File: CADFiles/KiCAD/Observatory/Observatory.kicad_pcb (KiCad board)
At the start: 2 copper layers, 204.4 x 77 mm, 49 parts, among them J1 GND/CUT, J10 Dio_Jump, J11 nRF Connections, J12 Sulu Header, J13 Dio_AD, J14 RsTx_Dio, J15 RsRx_Dio, J16 JScope Voltage, J17 WaveGen. 1 Mux Config., J18 JScope I+, J19 JScope I-, J2 Analog Discovery Connection, J20 Mounting Hole, J21 Mounting Hole, J22 Mounting Hole, J23 Mounting Hole, J24 prog. LED, J3 Digitial Discovery Connection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, J4 Scope 1 Mux Config., J5 Scope 2 Mux Config., J6 JScope V+, J7 JScope V-, J8 JScope Current IO, J9 5V_in, Q1 2N7002, U1 1, U2 Scope 1 Mux, U3 Wave Gen. Mux, U4 Scope 2 Mux

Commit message: Begin REV 2
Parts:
- removed 10k: 100k, Resistor_SMD:R_0805_2012Metric_Pad1.20x1.40mm_HandSolder
- removed J13: Dio_AD, Connector_PinHeader_2.54mm:PinHeader_2x16_P2.54mm_Vertical
- added R17: 100k, Resistor_SMD:R_0805_2012Metric_Pad1.20x1.40mm_HandSolder, F.Cu at (140.5, 31.5)
- added SW1: SW_DIP_x08, Button_Switch_THT:SW_DIP_SPSTx08_Slide_9.78x22.5mm_W7.62mm_P2.54mm, F.Cu at (210.5, 53.7)
- added SW2: SW_DIP_x08, Button_Switch_THT:SW_DIP_SPSTx08_Slide_9.78x22.5mm_W7.62mm_P2.54mm, F.Cu at (210.5, 83.5)
- added U5: Pico, 3rdPrty_Footprints:RPi_Pico_SMD_TH, B.Cu at (73.6, 90.5)
- J1: moved to F.Cu
- J16: value JScope Voltage -> JScope Voltage Select
- moved R13 160.0 mm to (217.8, 26.0), turned to -90 degrees
- moved R12 158.1 mm to (214.9, 26.0), turned to -90 degrees
- moved R11 156.5 mm to (211.9, 26.0), turned to -90 degrees
- moved R10 155.0 mm to (209.0, 26.0), turned to -90 degrees
- moved R9 153.7 mm to (206.1, 26.0), turned to -90 degrees
- moved R8 152.6 mm to (203.1, 26.0), turned to -90 degrees
- moved R7 151.8 mm to (200.2, 26.0), turned to -90 degrees
- moved R6 151.1 mm to (197.2, 26.0), turned to -90 degrees
- moved R5 150.6 mm to (194.3, 26.0), turned to -90 degrees
- moved R2 150.3 mm to (185.4, 26.0), turned to -90 degrees
- moved R4 150.3 mm to (191.3, 26.0), turned to -90 degrees
- moved R3 150.2 mm to (188.4, 26.0), turned to -90 degrees
- moved R16 122.6 mm to (182.4, 26.0), turned to -90 degrees
- moved R15 120.5 mm to (179.5, 26.0), turned to -90 degrees
- moved R14 118.6 mm to (176.6, 26.0), turned to -90 degrees
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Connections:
- J1 pad 1: JS_V- -> AD_Scope1-
- J10 pad 1: Scope 1 Mux  1 -> Scope 1 Mux  2
- J10 pad 2: DD_DIN_1 -> DD_DIN_0
- J10 pad 3: Scope 1 Mux  2 -> Scope 1 Mux  1
- J10 pad 4: DD_DIN_0 -> DD_DIN_1
- J11 pad 1: JS_V- -> AD_Scope1-
- J12 pad 1: JS_V- -> AD_Scope1-
- J12 pad 11: JS_V- -> AD_Scope1-
- J12 pad 2: JS_V- -> AD_Scope1-
- J12 pad 3: JS_V- -> AD_Scope1-
- J14 pad 2: DD_DIN_1 -> DD_DIN_0
- J15 pad 2: DD_DIN_0 -> DD_DIN_1
- J17 pad 1: JS_V- -> AD_Scope1-
- J17 pad 2: JS_V- -> AD_Scope1-
- J17 pad 3: JS_V- -> AD_Scope1-
- J17 pad 4: JS_V- -> AD_Scope1-
- J17 pad 5: JS_V- -> AD_Scope1-
- J2 pad 11: JS_V- -> AD_Scope1-
- J2 pad 12: JS_V- -> AD_Scope1-
- J2 pad 4: AD_Scope2- -> AD_Scope1-
- J2 pad 5: JS_V- -> AD_Scope1-
- J2 pad 6: JS_V- -> AD_Scope1-
- J3 pad 1: JS_V- -> AD_Scope1-
- J3 pad 11: JS_V- -> AD_Scope1-
- J3 pad 12: JS_V- -> AD_Scope1-
- J3 pad 2: JS_V- -> AD_Scope1-
- J3 pad 21: JS_V- -> AD_Scope1-
- J3 pad 22: JS_V- -> AD_Scope1-
- J3 pad 31: JS_V- -> AD_Scope1-
- J3 pad 32: JS_V- -> AD_Scope1-
- J4 pad 1: JS_V- -> AD_Scope1-
- J4 pad 2: JS_V- -> AD_Scope1-
- J4 pad 3: JS_V- -> AD_Scope1-
- J4 pad 4: JS_V- -> AD_Scope1-
- J4 pad 5: JS_V- -> AD_Scope1-
- J5 pad 1: JS_V- -> AD_Scope1-
- J5 pad 2: JS_V- -> AD_Scope1-
- J5 pad 3: JS_V- -> AD_Scope1-
- J5 pad 4: JS_V- -> AD_Scope1-
- J5 pad 5: JS_V- -> AD_Scope1-
- J7 pad 2: JS_V- -> AD_Scope1-
- J9 pad 1: JS_V- -> AD_Scope1-
- U1 pad 10b: JS_V- -> AD_Scope1-
- U1 pad 11c: JS_V- -> AD_Scope1-
- U1 pad 19a: JS_V- -> AD_Scope1-
- U1 pad 1a: JS_V- -> AD_Scope1-
- U1 pad 1c: JS_V- -> AD_Scope1-
- U1 pad 20a: JS_V- -> AD_Scope1-
- U1 pad 2c: JS_V- -> AD_Scope1-
- U1 pad 3b: JS_V- -> AD_Scope1-
- U1 pad 3c: JS_V- -> AD_Scope1-
- U2 pad 20: JS_V- -> AD_Scope1-
- U2 pad 21: JS_V- -> AD_Scope1-
- U2 pad 22: JS_V- -> AD_Scope1-
- U2 pad 23: JS_V- -> AD_Scope1-
- U2 pad 24: JS_V- -> AD_Scope1-
- U3 pad 1: Scope 1 Mux  1 -> Scopes Mux  1
- U3 pad 10: Scope 1 Mux  10 -> Scopes Mux  10
- U3 pad 11: Scope 1 Mux  11 -> Scopes Mux  11
- U3 pad 12: Scope 1 Mux  12 -> Scopes Mux  12
- U3 pad 2: Scope 1 Mux  2 -> Scopes Mux  2
- U3 pad 20: JS_V- -> AD_Scope1-
- U3 pad 21: JS_V- -> AD_Scope1-
- U3 pad 22: JS_V- -> AD_Scope1-
- U3 pad 23: JS_V- -> AD_Scope1-
- U3 pad 24: JS_V- -> AD_Scope1-
- U3 pad 3: Scope 1 Mux  3 -> Scopes Mux  3
- U3 pad 4: Scope 1 Mux  4 -> Scopes Mux  4
- U3 pad 45: Scope 1 Mux  16 -> Scopes Mux  16
- U3 pad 46: Scope 1 Mux  15 -> Scopes Mux  15
- U3 pad 47: Scope 1 Mux  14 -> Scopes Mux  14
- U3 pad 48: Scope 1 Mux  13 -> Scopes Mux  13
- U3 pad 5: Scope 1 Mux  5 -> Scopes Mux  5
- U3 pad 6: Scope 1 Mux  6 -> Scopes Mux  6
- U3 pad 7: Scope 1 Mux  7 -> Scopes Mux  7
- U3 pad 8: Scope 1 Mux  8 -> Scopes Mux  8
- U3 pad 9: Scope 1 Mux  9 -> Scopes Mux  9
- U4 pad 20: JS_V- -> AD_Scope1-
- U4 pad 21: JS_V- -> AD_Scope1-
- U4 pad 22: JS_V- -> AD_Scope1-
- U4 pad 23: JS_V- -> AD_Scope1-
- U4 pad 24: JS_V- -> AD_Scope1-
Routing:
- net +5V: track 276.4 -> 0.00 mm, vias 15 -> 0
- net AD_Scope1+: track 228.5 -> 0.00 mm, vias 2 -> 0
- net Scope 1 Mux  12: track 225.2 -> 0.00 mm, vias 2 -> 0
- net AD_Scope2+: track 220.7 -> 0.00 mm, vias 2 -> 0
- net Scope 1 Mux  11: track 218.4 -> 0.00 mm, vias 2 -> 0
- net Scope 1 Mux  10: track 216.7 -> 0.00 mm, vias 2 -> 0
- net Scope 1 Mux  9: track 209.4 -> 0.00 mm, vias 2 -> 0
- net Scope 1 Mux  8: track 208.7 -> 0.00 mm, vias 2 -> 0
- net Scope 1 Mux  7: track 202.1 -> 0.00 mm, vias 2 -> 0
- net Scope 1 Mux  6: track 201.1 -> 0.00 mm, vias 2 -> 0
- net Scope 1 Mux  5: track 194.6 -> 0.00 mm, vias 2 -> 0
- net Scope 1 Mux  4: track 194.2 -> 0.00 mm, vias 2 -> 0
- net Scope 1 Mux  2: track 191.5 -> 0.00 mm, vias 2 -> 0
- net Scope 1 Mux  3: track 189.9 -> 0.00 mm, vias 2 -> 0
- net Scope 1 Mux  16: track 188.7 -> 0.00 mm, vias 4 -> 0
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- removed copper zone on B.Cu, net JS_V-
- removed copper zone on F.Cu, net JS_V-
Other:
- copper layers 2 -> 4
- board text removed: "+"
- board text removed: "-"
- board text removed: "->"
- board text removed: "1.1V"
- board text removed: "1.1V_IN"
- board text removed: "1.8V"
- board text removed: "3WB CLK"
- board text removed: "3WB DATA"
- board text removed: "3WB ENB"
- board text removed: "ADC IN"
- board text removed: "ADC OUT"
- board text removed: "BTSRC SEL"
- board text removed: "GND"
- board text removed: "HARD RESET"
- board text removed: "IMU VDD"
- board text removed: "IMU VDDIO"
- board text removed: "JScope Voltage"
- board text removed: "NRF GND"
- board text removed: "NRF VDDD"
- board text removed: "Single-Chip micro Mote Observatory"
- board text removed: "VBAT"
- board text removed: "VDDD"
- board text removed: "VDDIO"

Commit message: All nets routed.
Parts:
- added J13: Serial, Connector_PinHeader_2.54mm:PinHeader_1x02_P2.54mm_Vertical, F.Cu at (93.5, 107.9)
- C1, C2, J1, Q1, R1, R17: moved to B.Cu
- J16: value JScope Voltage Select -> JScope Voltage
- J17, J4, J5: footprint Imports:DIP8_208-5_CTS -> Button_Switch_SMD:SW_DIP_SPSTx05_Slide_6.7x14.26mm_W8.61mm_P2.54mm_LowProfile
- SW1, SW2: footprint Button_Switch_THT:SW_DIP_SPSTx08_Slide_9.78x22.5mm_W7.62mm_P2.54mm -> Button_Switch_SMD:SW_DIP_SPSTx08_Slide_6.7x21.88mm_W8.61mm_P2.54mm_LowProfile
- moved G*** 150.9 mm to (125.8, 78.1)
- moved U5 142.7 mm to (213.4, 61.9), turned to 180 degrees
- moved J4 117.6 mm to (151.1, 42.3), turned to -90 degrees
- moved R13 98.9 mm to (122.0, 50.2), turned to 90 degrees
- moved J5 93.8 mm to (134.6, 42.3), turned to -90 degrees
- moved R12 92.6 mm to (125.5, 50.2), turned to 90 degrees
- moved R11 86.7 mm to (128.7, 50.2), turned to 90 degrees
- moved R10 81.0 mm to (131.7, 50.2), turned to 90 degrees
- moved J1 78.4 mm to (75.3, 46.6), turned to 180 degrees
- moved J23 77.1 mm to (250.2, 40.2)
- moved R9 75.4 mm to (134.6, 50.2), turned to 90 degrees
- moved Q1 74.4 mm to (76.0, 50.2)
- moved R16 74.1 mm to (112.4, 50.1), turned to 90 degrees
- moved C1 73.2 mm to (71.4, 46.6), turned to 180 degrees
- moved C2 73.0 mm to (71.4, 49.0), turned to 180 degrees
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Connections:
- J1 pad 1: AD_Scope1- -> AD_DC_Supply-
- J10 pad 1: Scope 1 Mux  2 -> Scope 1 Mux  1
- J10 pad 13: Scope 1 Mux  7 -> Scope 1 Mux  12
- J10 pad 15: Scope 1 Mux  8 -> Scope 1 Mux  11
- J10 pad 17: Scope 1 Mux  9 -> Scope 1 Mux  10
- J10 pad 19: Scope 1 Mux  10 -> Scope 1 Mux  9
- J10 pad 21: Scope 1 Mux  11 -> Scope 1 Mux  8
- J10 pad 23: Scope 1 Mux  12 -> Scope 1 Mux  7
- J10 pad 3: Scope 1 Mux  1 -> Scope 1 Mux  2
- J11 pad 1: AD_Scope1- -> AD_DC_Supply-
- J12 pad 1: AD_Scope1- -> AD_DC_Supply-
- J12 pad 11: AD_Scope1- -> AD_DC_Supply-
- J12 pad 12: +5V -> AD_DC_Supply+
- J12 pad 2: AD_Scope1- -> AD_DC_Supply-
- J12 pad 3: AD_Scope1- -> AD_DC_Supply-
- J16 pad 5: +5V -> AD_DC_Supply+
- J17 pad 1: AD_Scope1- -> AD_DC_Supply-
- J17 pad 2: AD_Scope1- -> AD_DC_Supply-
- J17 pad 3: AD_Scope1- -> AD_DC_Supply-
- J17 pad 4: AD_Scope1- -> AD_DC_Supply-
- J17 pad 5: AD_Scope1- -> AD_DC_Supply-
- J2 pad 11: AD_Scope1- -> AD_DC_Supply-
- J2 pad 12: AD_Scope1- -> AD_DC_Supply-
- J2 pad 2: AD_Scope1- -> AD_DC_Supply-
- J2 pad 4: AD_Scope1- -> AD_DC_Supply-
- J2 pad 5: AD_Scope1- -> AD_DC_Supply-
- J2 pad 6: AD_Scope1- -> AD_DC_Supply-
- J3 pad 1: AD_Scope1- -> AD_DC_Supply-
- J3 pad 11: AD_Scope1- -> AD_DC_Supply-
- J3 pad 12: AD_Scope1- -> AD_DC_Supply-
- J3 pad 2: AD_Scope1- -> AD_DC_Supply-
- J3 pad 21: AD_Scope1- -> AD_DC_Supply-
- J3 pad 22: AD_Scope1- -> AD_DC_Supply-
- J3 pad 31: AD_Scope1- -> AD_DC_Supply-
- J3 pad 32: AD_Scope1- -> AD_DC_Supply-
- J4 pad 1: AD_Scope1- -> AD_DC_Supply-
- J4 pad 2: AD_Scope1- -> AD_DC_Supply-
- J4 pad 3: AD_Scope1- -> AD_DC_Supply-
- J4 pad 4: AD_Scope1- -> AD_DC_Supply-
- J4 pad 5: AD_Scope1- -> AD_DC_Supply-
- J5 pad 1: AD_Scope1- -> AD_DC_Supply-
- J5 pad 2: AD_Scope1- -> AD_DC_Supply-
- J5 pad 3: AD_Scope1- -> AD_DC_Supply-
- J5 pad 4: AD_Scope1- -> AD_DC_Supply-
- J5 pad 5: AD_Scope1- -> AD_DC_Supply-
- J7 pad 2: AD_Scope1- -> AD_DC_Supply-
- J9 pad 1: AD_Scope1- -> AD_DC_Supply-
- J9 pad 2: +5V -> AD_DC_Supply+
- R10 pad 1: +5V -> AD_DC_Supply+
- R11 pad 1: +5V -> AD_DC_Supply+
- R12 pad 1: +5V -> AD_DC_Supply+
- R13 pad 1: +5V -> AD_DC_Supply+
- R14 pad 1: +5V -> AD_DC_Supply+
- R15 pad 1: +5V -> AD_DC_Supply+
- R16 pad 1: +5V -> AD_DC_Supply+
- R2 pad 1: +5V -> AD_DC_Supply+
- R3 pad 1: +5V -> AD_DC_Supply+
- R4 pad 1: +5V -> AD_DC_Supply+
- R5 pad 1: +5V -> AD_DC_Supply+
- R6 pad 1: +5V -> AD_DC_Supply+
- R7 pad 1: +5V -> AD_DC_Supply+
- R8 pad 1: +5V -> AD_DC_Supply+
- R9 pad 1: +5V -> AD_DC_Supply+
- SW2 pad 10: AD_DIO_14 -> AD_DIO_9
- SW2 pad 11: AD_DIO_13 -> AD_DIO_10
- SW2 pad 12: AD_DIO_12 -> AD_DIO_11
- SW2 pad 13: AD_DIO_11 -> AD_DIO_12
- SW2 pad 14: AD_DIO_10 -> AD_DIO_13
- SW2 pad 15: AD_DIO_9 -> AD_DIO_14
- SW2 pad 16: AD_DIO_8 -> AD_DIO_15
- SW2 pad 9: AD_DIO_15 -> AD_DIO_8
- U1 pad 10a: Scope 1 Mux  8 -> Scope 1 Mux  11
- U1 pad 10b: AD_Scope1- -> AD_DC_Supply-
- U1 pad 11a: Scope 1 Mux  9 -> Scope 1 Mux  10
- U1 pad 11c: AD_Scope1- -> AD_DC_Supply-
- U1 pad 12a: Scope 1 Mux  10 -> Scope 1 Mux  9
- U1 pad 12c: +5V -> AD_DC_Supply+
- U1 pad 13a: Scope 1 Mux  11 -> Scope 1 Mux  8
- U1 pad 14a: Scope 1 Mux  12 -> Scope 1 Mux  7
- U1 pad 19a: AD_Scope1- -> AD_DC_Supply-
- U1 pad 1a: AD_Scope1- -> AD_DC_Supply-
- U1 pad 1c: AD_Scope1- -> AD_DC_Supply-
- U1 pad 20a: AD_Scope1- -> AD_DC_Supply-
- U1 pad 2c: AD_Scope1- -> AD_DC_Supply-
- U1 pad 3b: AD_Scope1- -> AD_DC_Supply-
- U1 pad 3c: AD_Scope1- -> AD_DC_Supply-
- U1 pad 9a: Scope 1 Mux  7 -> Scope 1 Mux  12
- U2 pad 13: +5V -> AD_DC_Supply+
- U2 pad 14: +5V -> AD_DC_Supply+
- U2 pad 20: AD_Scope1- -> AD_DC_Supply-
- U2 pad 21: AD_Scope1- -> AD_DC_Supply-
- U2 pad 22: AD_Scope1- -> AD_DC_Supply-
- U2 pad 23: AD_Scope1- -> AD_DC_Supply-
- U2 pad 24: AD_Scope1- -> AD_DC_Supply-
- U2 pad 43: AD_Scope1+ -> AD_Scope2+
- U3 pad 1: Scopes Mux  1 -> Scope 1 Mux  1
- U3 pad 10: Scopes Mux  10 -> Scope 1 Mux  9
- U3 pad 11: Scopes Mux  11 -> Scope 1 Mux  8
- U3 pad 12: Scopes Mux  12 -> Scope 1 Mux  7
- U3 pad 13: +5V -> AD_DC_Supply+
- U3 pad 14: +5V -> AD_DC_Supply+
- U3 pad 2: Scopes Mux  2 -> Scope 1 Mux  2
- U3 pad 20: AD_Scope1- -> AD_DC_Supply-
- U3 pad 21: AD_Scope1- -> AD_DC_Supply-
- U3 pad 22: AD_Scope1- -> AD_DC_Supply-
- U3 pad 23: AD_Scope1- -> AD_DC_Supply-
- U3 pad 24: AD_Scope1- -> AD_DC_Supply-
- U3 pad 3: Scopes Mux  3 -> Scope 1 Mux  3
- U3 pad 4: Scopes Mux  4 -> Scope 1 Mux  4
- U3 pad 43: AD_WaveGen1 -> AD_WaveGen2
- U3 pad 45: Scopes Mux  16 -> Scope 1 Mux  13
- U3 pad 46: Scopes Mux  15 -> Scope 1 Mux  14
- U3 pad 47: Scopes Mux  14 -> Scope 1 Mux  15
- U3 pad 48: Scopes Mux  13 -> Scope 1 Mux  16
- U3 pad 5: Scopes Mux  5 -> Scope 1 Mux  5
- U3 pad 6: Scopes Mux  6 -> Scope 1 Mux  6
- U3 pad 7: Scopes Mux  7 -> Scope 1 Mux  12
- U3 pad 8: Scopes Mux  8 -> Scope 1 Mux  11
- U3 pad 9: Scopes Mux  9 -> Scope 1 Mux  10
- U4 pad 13: +5V -> AD_DC_Supply+
- U4 pad 14: +5V -> AD_DC_Supply+
- U4 pad 20: AD_Scope1- -> AD_DC_Supply-
- U4 pad 21: AD_Scope1- -> AD_DC_Supply-
- U4 pad 22: AD_Scope1- -> AD_DC_Supply-
- U4 pad 23: AD_Scope1- -> AD_DC_Supply-
- U4 pad 24: AD_Scope1- -> AD_DC_Supply-
- U4 pad 37: Scope 1 Mux  13 -> Scope 1 Mux  16
- U4 pad 38: Scope 1 Mux  14 -> Scope 1 Mux  15
- U4 pad 39: Scope 1 Mux  15 -> Scope 1 Mux  14
- U4 pad 40: Scope 1 Mux  16 -> Scope 1 Mux  13
- U4 pad 43: AD_Scope2+ -> AD_Scope1+
- U5 pad 1: Scope 1 Mux Control 0 -> unconnected-(U5-GPIO0-Pad1)
- U5 pad 10: Scope 2 Mux Control 2 -> unconnected-(U5-GPIO7-Pad10)
- U5 pad 11: Scope 2 Mux Control 3 -> unconnected-(U5-GPIO8-Pad11)
- U5 pad 13: AD_Scope1- -> AD_DC_Supply-
- U5 pad 14: WaveGen. Mux Control 0 -> WaveGen. Mux Control 4
- U5 pad 15: WaveGen. Mux Control 1 -> WaveGen. Mux Control 3
- U5 pad 17: WaveGen. Mux Control 3 -> WaveGen. Mux Control 1
- U5 pad 18: AD_Scope1- -> AD_DC_Supply-
- U5 pad 19: WaveGen. Mux Control 4 -> WaveGen. Mux Control 0
- U5 pad 2: Scope 1 Mux Control 1 -> unconnected-(U5-GPIO1-Pad2)
- U5 pad 21: unconnected-(U5-GPIO16-Pad21) -> Scope 2 Mux Control 3
- U5 pad 22: unconnected-(U5-GPIO17-Pad22) -> Scope 2 Mux Control 2
- U5 pad 23: AD_Scope1- -> AD_DC_Supply-
- U5 pad 24: unconnected-(U5-GPIO18-Pad24) -> Scope 2 Mux Control 1
- U5 pad 25: unconnected-(U5-GPIO19-Pad25) -> Scope 2 Mux Control 0
- U5 pad 26: unconnected-(U5-GPIO20-Pad26) -> Scope 1 Mux Control 0
- U5 pad 27: unconnected-(U5-GPIO21-Pad27) -> Scope 1 Mux Control 1
- U5 pad 28: AD_Scope1- -> AD_DC_Supply-
- U5 pad 29: unconnected-(U5-GPIO22-Pad29) -> Scope 1 Mux Control 2
- U5 pad 3: AD_Scope1- -> AD_DC_Supply-
- U5 pad 31: unconnected-(U5-GPIO26_ADC0-Pad31) -> Scope 1 Mux Control 3
- U5 pad 32: unconnected-(U5-GPIO27_ADC1-Pad32) -> Scope 1 Mux Control 4
- U5 pad 33: AD_Scope1- -> AD_DC_Supply-
- U5 pad 38: AD_Scope1- -> AD_DC_Supply-
- U5 pad 39: +5V -> AD_DC_Supply+
- U5 pad 4: Scope 1 Mux Control 2 -> unconnected-(U5-GPIO2-Pad4)
- U5 pad 5: Scope 1 Mux Control 3 -> unconnected-(U5-GPIO3-Pad5)
- U5 pad 6: Scope 1 Mux Control 4 -> unconnected-(U5-GPIO4-Pad6)
- U5 pad 7: Scope 2 Mux Control 0 -> unconnected-(U5-GPIO5-Pad7)
- U5 pad 8: AD_Scope1- -> AD_DC_Supply-
- U5 pad 9: Scope 2 Mux Control 1 -> unconnected-(U5-GPIO6-Pad9)
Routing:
- net AD_Scope2+: track 0.00 -> 226.3 mm
- net AD_WaveGen2: track 0.00 -> 195.0 mm
- net AD_Scope1+: track 0.00 -> 187.9 mm
- net WaveGen. Mux Control 4: track 0.00 -> 184.7 mm, vias 0 -> 1
- net WaveGen. Mux Control 3: track 0.00 -> 182.8 mm, vias 0 -> 1
- net WaveGen. Mux Control 2: track 0.00 -> 179.9 mm, vias 0 -> 1
- net WaveGen. Mux Control 1: track 0.58 -> 177.5 mm, vias 0 -> 1
- net WaveGen. Mux Control 0: track 0.00 -> 173.4 mm, vias 0 -> 1
- net Scope 2 Mux Control 4: track 0.00 -> 166.1 mm, vias 0 -> 2
- net Scope 2 Mux Control 3: track 0.00 -> 151.7 mm, vias 0 -> 2
- net Scope 1 Mux  13: track 0.00 -> 148.7 mm, vias 0 -> 4
- net Scope 2 Mux Control 2: track 0.00 -> 148.5 mm, vias 0 -> 2
- net Scope 1 Mux  14: track 0.00 -> 147.5 mm, vias 0 -> 3
- net Scope 1 Mux  15: track 0.00 -> 145.7 mm, vias 0 -> 4
- net Scope 1 Mux  16: track 0.00 -> 145.0 mm, vias 0 -> 4
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- added copper zone on In2.Cu, net AD_DC_Supply+
- added copper zone on B.Cu, net AD_DC_Supply-
- added copper zone on In1.Cu, net AD_DC_Supply-
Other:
- board size 204.4 x 77 mm -> 213.4 x 78.5 mm
- board text removed: "EXT_BAT"

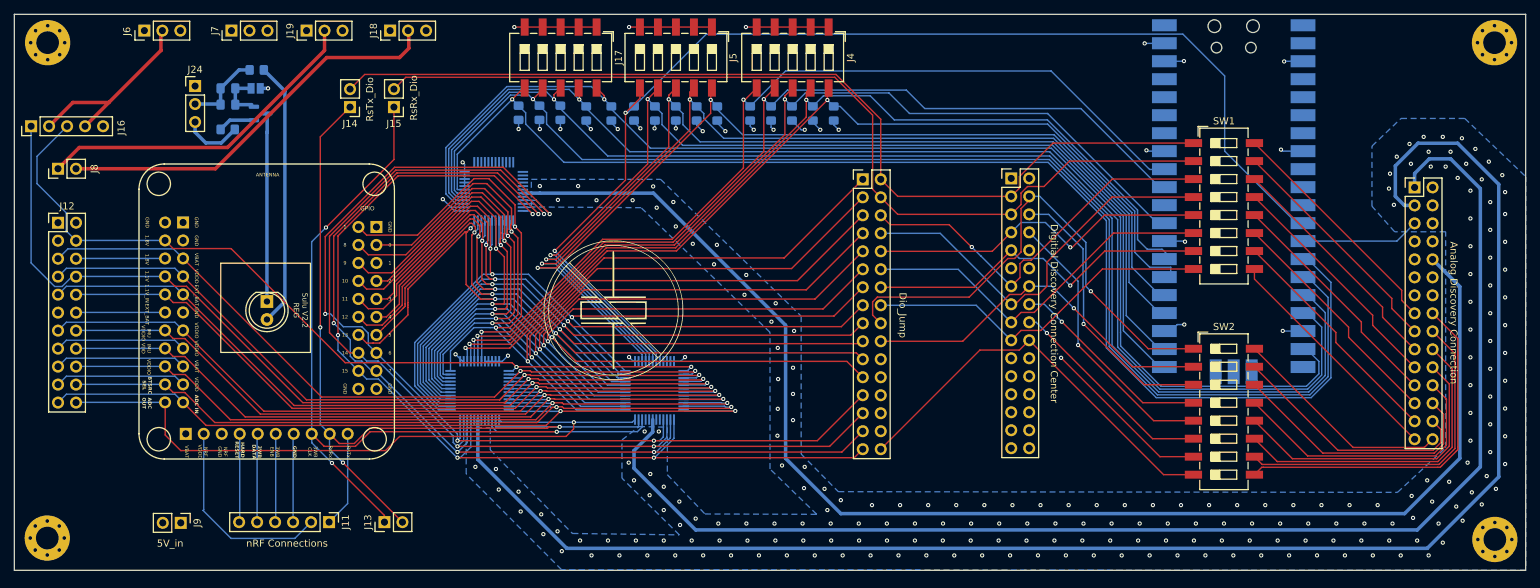
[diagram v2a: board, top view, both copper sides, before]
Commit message: DRC pass. Labels Added.
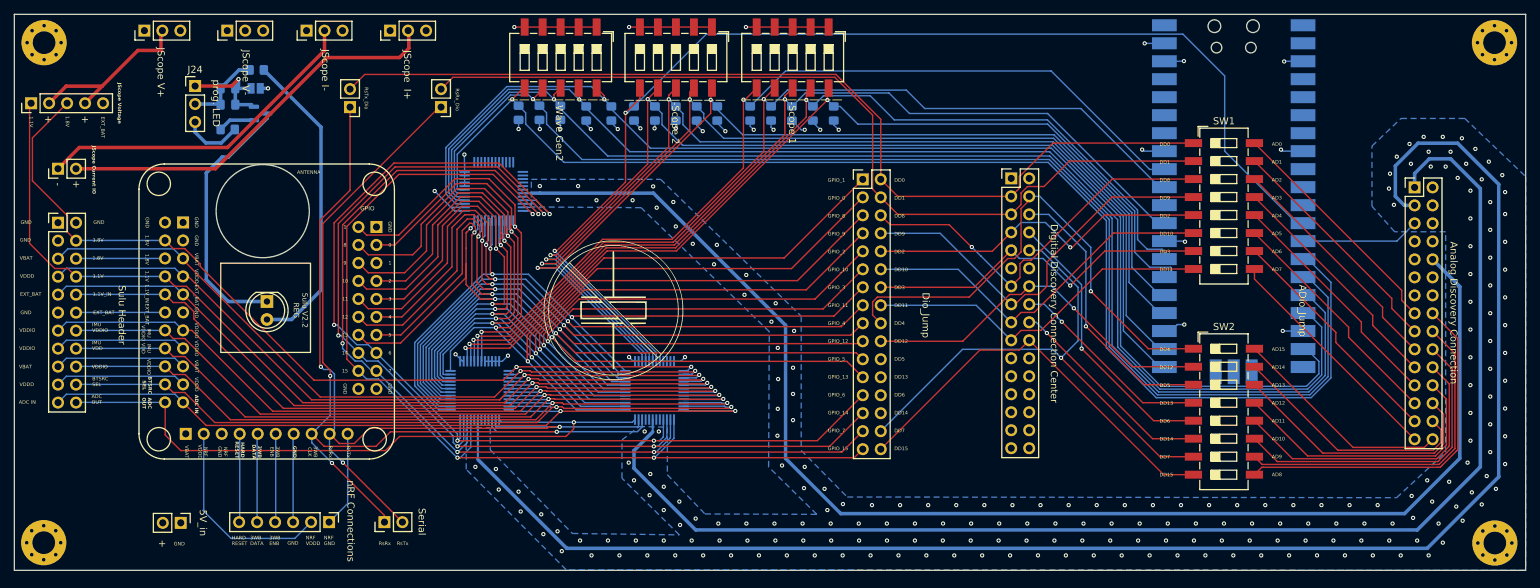
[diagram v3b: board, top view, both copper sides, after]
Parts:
- moved J15 6.65 mm to (101.5, 49.3)
- moved J16 3.25 mm to (43.6, 48.8)
- moved J20 0.82 mm to (45.4, 110.8)
- moved J7 0.60 mm to (71.3, 38.5)
- moved J21 0.50 mm to (45.4, 40.2)
- moved J22 0.50 mm to (250.2, 110.8)
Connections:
- U2 pad 40: Scope 1 Mux  32 -> unconnected-(U2-S32-Pad40)
- U4 pad 45: Scope 1 Mux  32 -> unconnected-(U4-S16-Pad45)
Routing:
- net Net-(Q1-D): track 26.6 -> 37.4 mm
- net Net-(J1-Pin_2): track 7.27 -> 15.3 mm, vias 0 -> 1
- net DD_DIN_1: track 131.8 -> 125.2 mm
- net Net-(U1-2_led): track 37.5 -> 43.8 mm
- net Scope 1 Mux  17: track 117.1 -> 122.6 mm
- net DD_DIN_7: track 70.1 -> 75.2 mm
- net Scope 1 Mux  31: track 127.7 -> 131.5 mm
- net Scope 1 Mux  7: track 129.2 -> 126.2 mm
- net JS_V+: track 27.9 -> 25.2 mm
- net Scope 1 Mux  6: track 136.0 -> 138.7 mm
- net Scope 1 Mux  5: track 134.6 -> 137.0 mm
- net Scope 1 Mux  4: track 139.8 -> 142.0 mm
- net Scope 1 Mux  11: track 132.6 -> 134.6 mm
- net Scope 1 Mux  12: track 129.8 -> 131.9 mm
- net Scope 1 Mux  8: track 126.4 -> 128.4 mm
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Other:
- outline, holes or cut-outs redrawn
- board text added: "+"
- board text added: "-"
- board text added: "1.1V"
- board text added: "1.1V_IN"
- board text added: "1.8V"
- board text added: "3WB DATA"
- board text added: "3WB ENB"
- board text added: "AD0"
- board text added: "AD1"
- board text added: "AD10"
- board text added: "AD11"
- board text added: "AD12"
- board text added: "AD13"
- board text added: "AD14"
- board text added: "AD15"
- board text added: "AD2"
- board text added: "AD3"
- board text added: "AD4"
- board text added: "AD5"
- board text added: "AD6"
- board text added: "AD7"
- board text added: "AD8"
- board text added: "AD9"
- board text added: "ADC IN"
- board text added: "ADC OUT"
- board text added: "ADio_Jump"
- board text added: "BTSRC SEL"
- board text added: "DD0"
- board text added: "DD1"
- board text added: "DD10"
- board text added: "DD11"
- board text added: "DD12"
- board text added: "DD13"
- board text added: "DD14"
- board text added: "DD15"
- board text added: "DD2"
- board text added: "DD3"
- board text added: "DD4"
- board text added: "DD5"
- board text added: "DD6"
- board text added: "DD7"
- board text added: "DD8"
- board text added: "DD9"
- board text added: "EXT_BAT"
- board text added: "GND"
- board text added: "GPIO_0"
- board text added: "GPIO_1"
- board text added: "GPIO_10"
- board text added: "GPIO_11"
- board text added: "GPIO_12"
- board text added: "GPIO_13"
- board text added: "GPIO_14"
- board text added: "GPIO_15"
- board text added: "GPIO_2"
- board text added: "GPIO_3"
- board text added: "GPIO_4"
- board text added: "GPIO_5"
- board text added: "GPIO_6"
- board text added: "GPIO_7"
- board text added: "GPIO_8"
- board text added: "GPIO_9"
- board text added: "HARD RESET"
- board text added: "IMU VDD"
- board text added: "IMU VDDIO"
- board text added: "NRF GND"
- board text added: "NRF VDDD"
- board text added: "RsRx"
- board text added: "RsTx"
- board text added: "VBAT"
- board text added: "VDDD"
- board text added: "VDDIO"
- board text added: "| | | | |-Scope 1 | | | |"
- board text added: "| | | | |-Scope 2 | | | |"
- board text added: "| | | | |-Wave Gen2 | | | |"

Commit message: ADD REV2 PDFs
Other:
- board text added: "WEST LAB CAPSTONE SCUM OBSERVATORY REV2"
- board text removed: "WEST LAB CAPSTONE SCUM OBSERVATORY REV1"
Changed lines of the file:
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@@
 	)
 	(footprint "Connector_PinHeader_2.54mm:PinHeader_2x11_P2.54mm_Vertical"
-		(locked yes)
 		(layer "F.Cu")
 		(at 47.368999 65.62)
@@
 	)
 	(footprint "Connector_PinHeader_2.54mm:PinHeader_2x15_P2.54mm_Vertical"
-		(locked yes)
 		(layer "F.Cu")
 		(at 238.92 60.637)
@@
 	)
 	(footprint "3rdPrty_Footprints:SuLu_Foot"
-		(locked yes)
 		(layer "F.Cu")
 		(at 76.768999 77.988 -90)
@@
 		)
 	)
-	(gr_text "WEST LAB CAPSTONE SCUM OBSERVATORY REV1"
+	(gr_text "WEST LAB CAPSTONE SCUM OBSERVATORY REV2"
 		(at 247.95 93.35 270)
 		(layer "B.SilkS")
